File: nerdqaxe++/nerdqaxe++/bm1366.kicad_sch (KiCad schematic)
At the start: 82 parts, among them U19 BM1370_mode1, U20 BM1370, U25 BM1370_mode1, U26 BM1370_mode1, U6 SN74AVC4T774, U8 25MHz

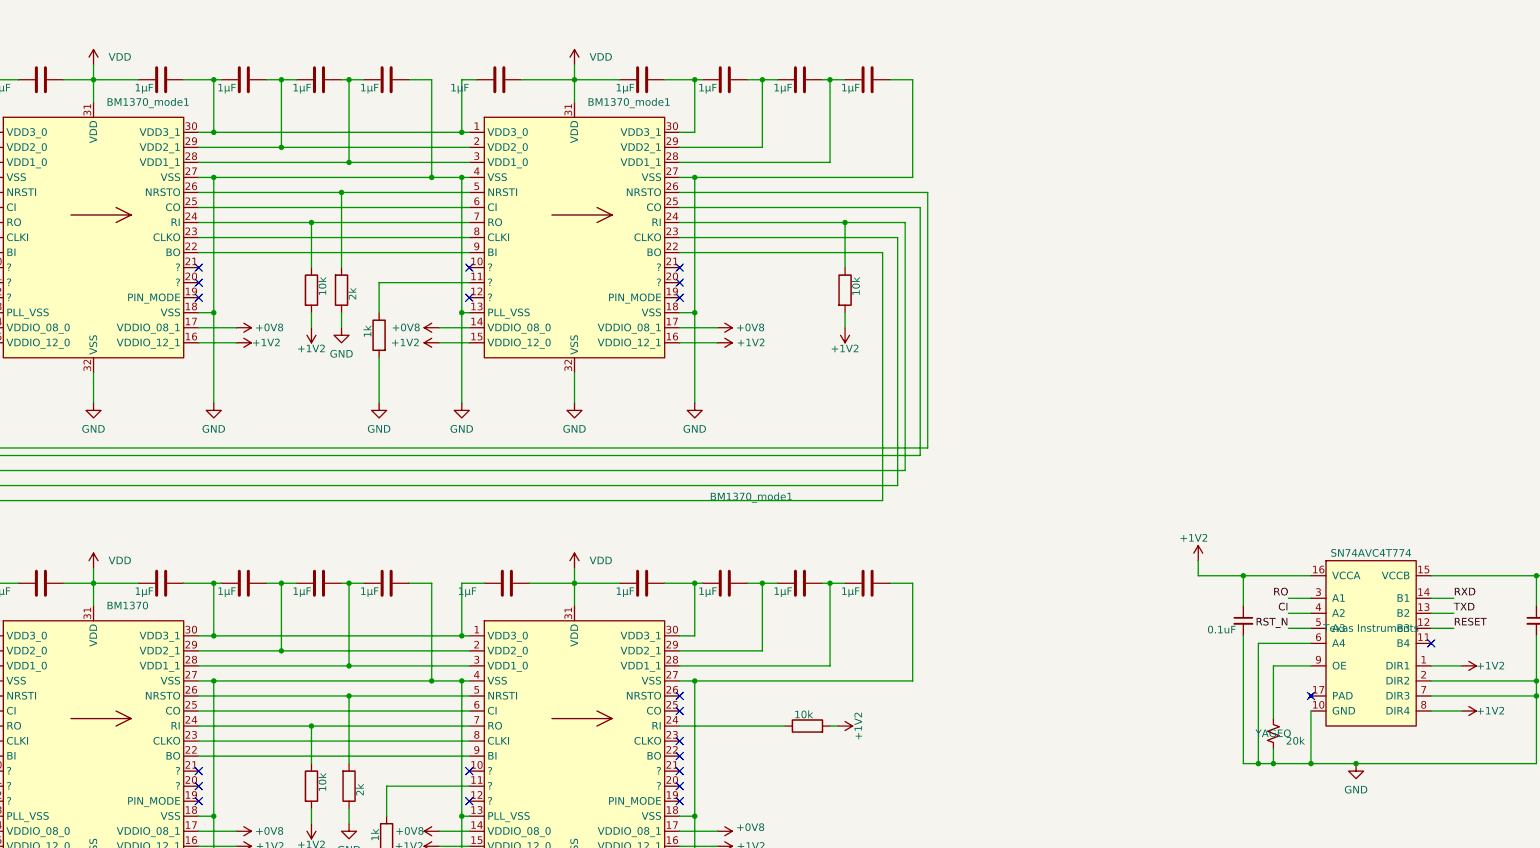
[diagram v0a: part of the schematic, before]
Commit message: Edit on rev 6.1PM
- Moved XT30 connector to the back of the board
- Edited VDD polygon
- Fixed various via placements
- Fixed various tracing
- Updated BM1370 footprint and solder paste stencil
- Updated CSD95472Q5MC footprint and solder paste stencil
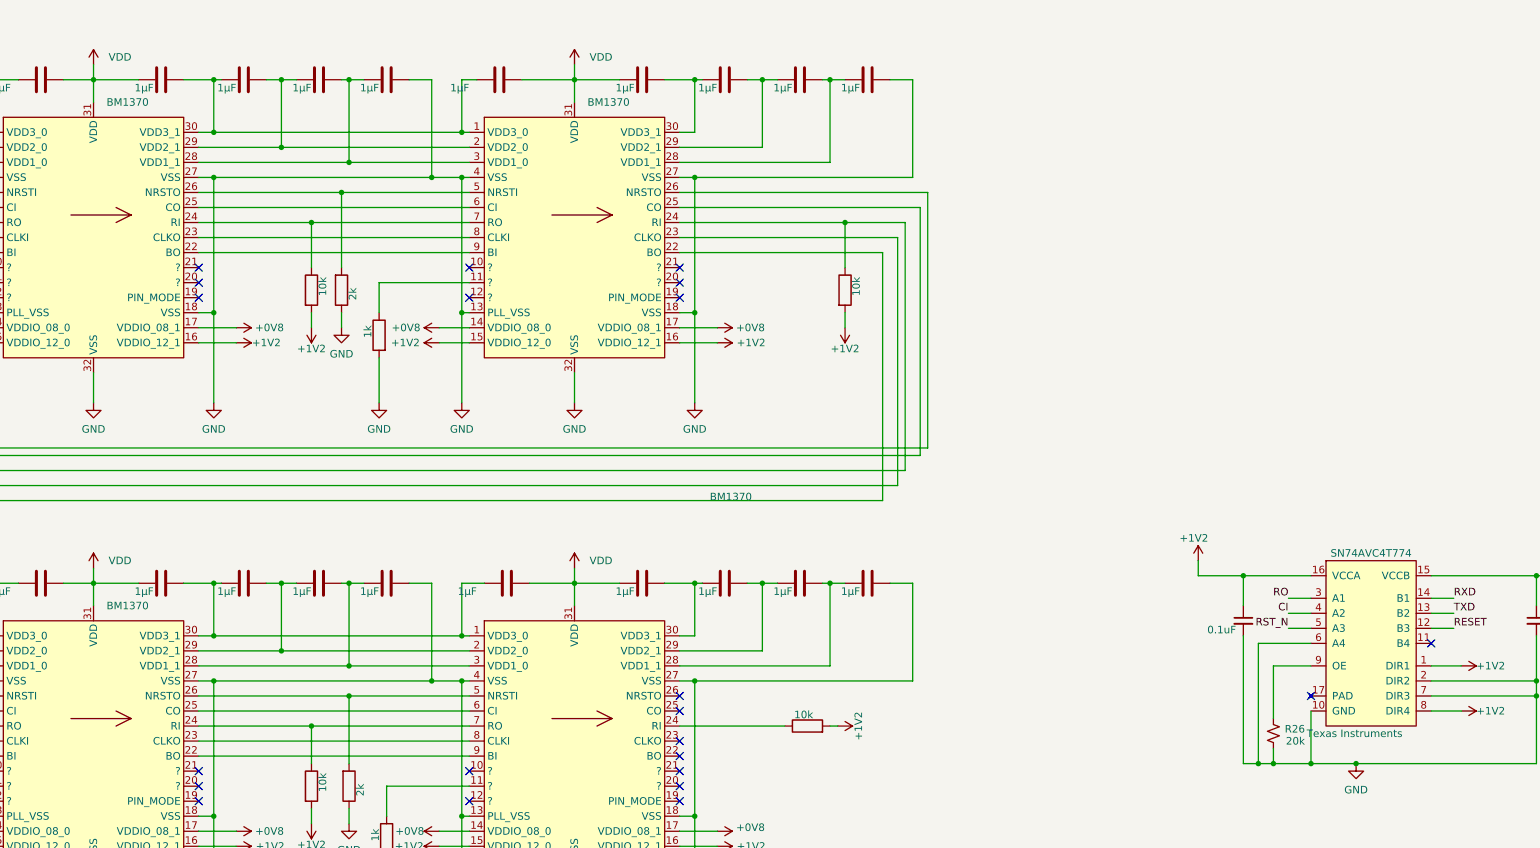
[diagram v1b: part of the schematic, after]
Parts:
- C100, C59: Manufacturer (none) -> KYOCERA AVX
- U19, U25, U26: value BM1370_mode1 -> BM1370; footprint qaxe:BM1370 -> qaxe:BM1370_paste; Manufacturer  (none) -> BITMAIN; PARTNO (none) -> BM1370
- U20: footprint qaxe:BM1370 -> qaxe:BM1370_paste; Manufacturer  (none) -> BITMAIN; PARTNO (none) -> BM1370
